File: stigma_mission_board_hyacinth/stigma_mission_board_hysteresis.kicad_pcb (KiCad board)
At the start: 4 copper layers, 50 x 150 mm, 205 parts, among them J1 DF40C-70DS-0.4V(51), J2 DF40HB(2.5)-10DS-0.4V(51), J7 SMA, J8 SMA, J9 JST-GH 4Pin, Q1 DMN2056U, Q2 DMN2056U, Q3 AOSP21321, Q4 DMN2056U, Q5 AOSP21321, Q6 DMN2056U, Q7 AOSP21321, Q8 DMN2056U, Q9 AOSP21321, U1 LAN8742A, U10 MCP2562-E-SN, U11 MCP2562-E-SN, U12 SN74HCS594, U13 INA181, U14 INA181, U15 INA181, U16 INA181, U2 INA181, U3 TPD4E1U06, U4 L7805, U5 L7805, U6 AZ1117H-ADJ, U7 AZ1117H-ADJ, U8 Ai-Thinker-Ra-01, U9 Ai-Thinker-Ra-01, Y1 25MHz

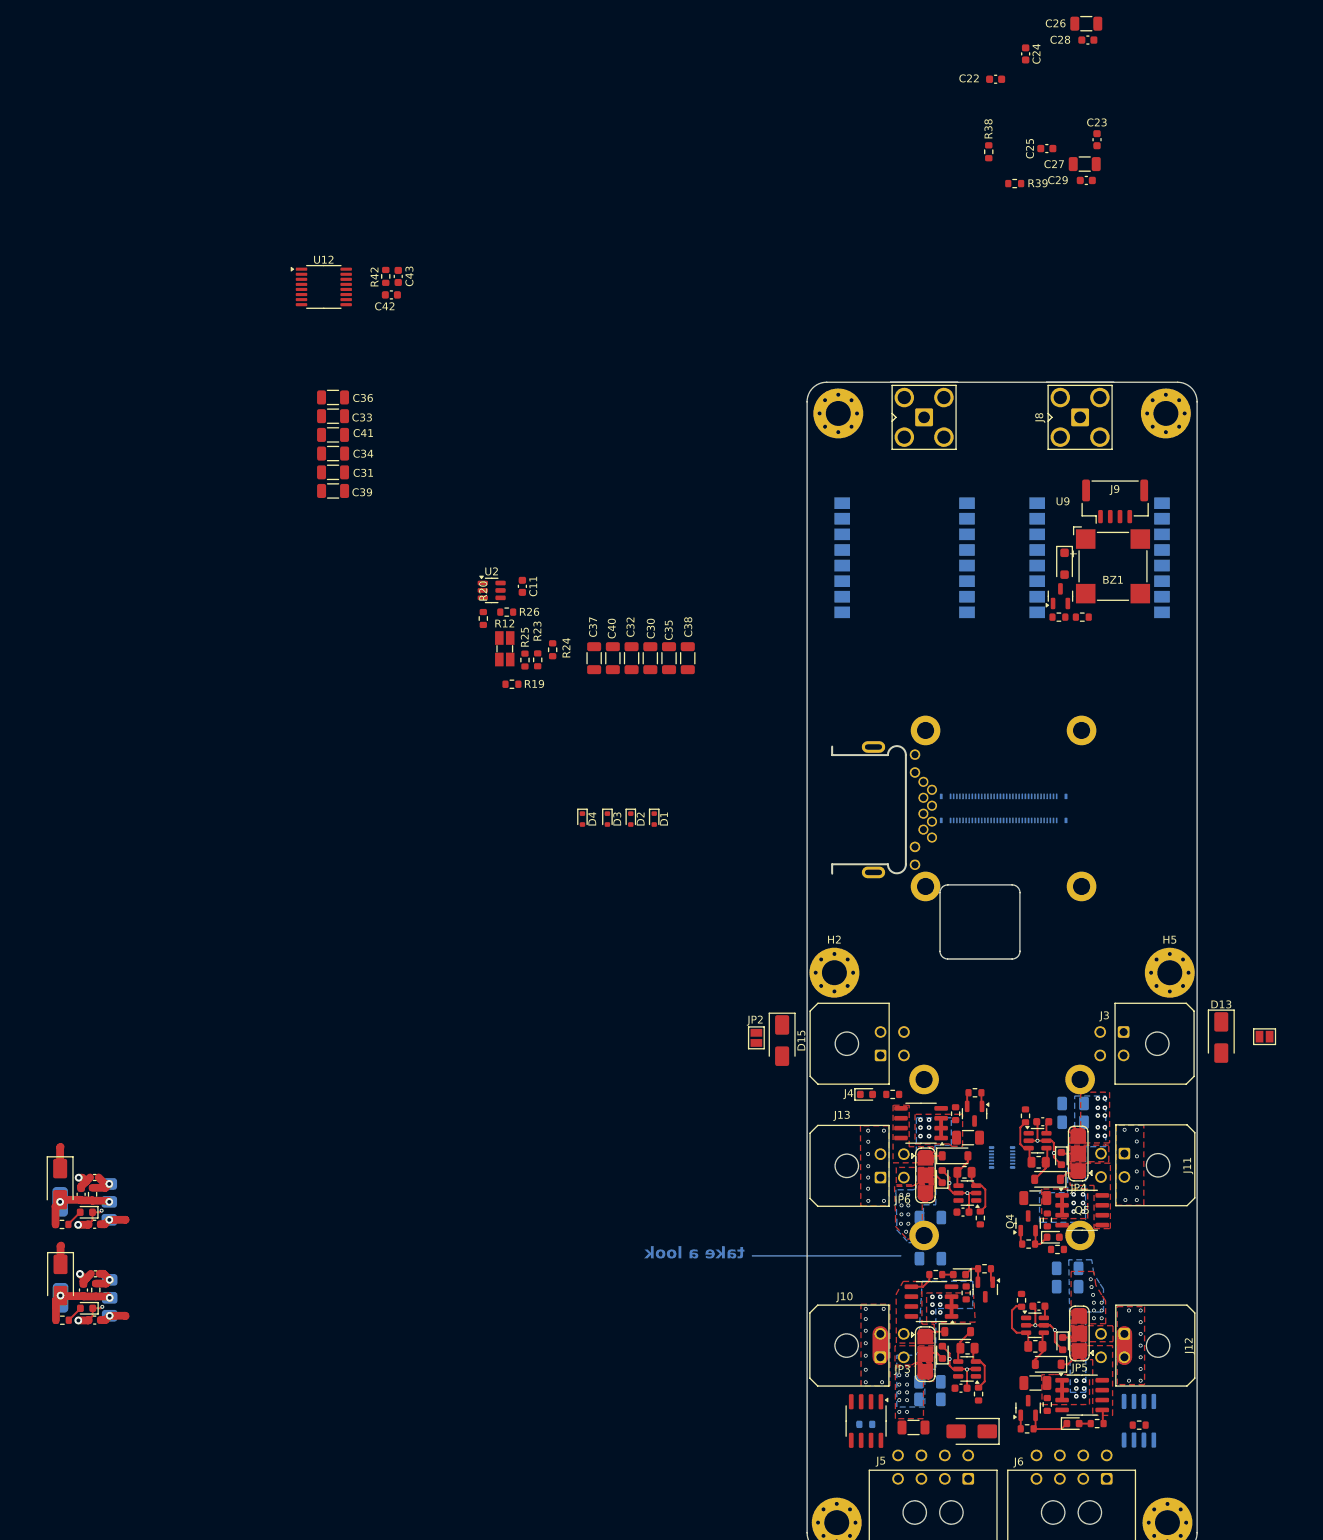
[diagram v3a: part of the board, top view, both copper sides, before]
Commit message: Layed out 3.3v regulators, buzzer, shift register and current + voltage sensing on the mission board pcb
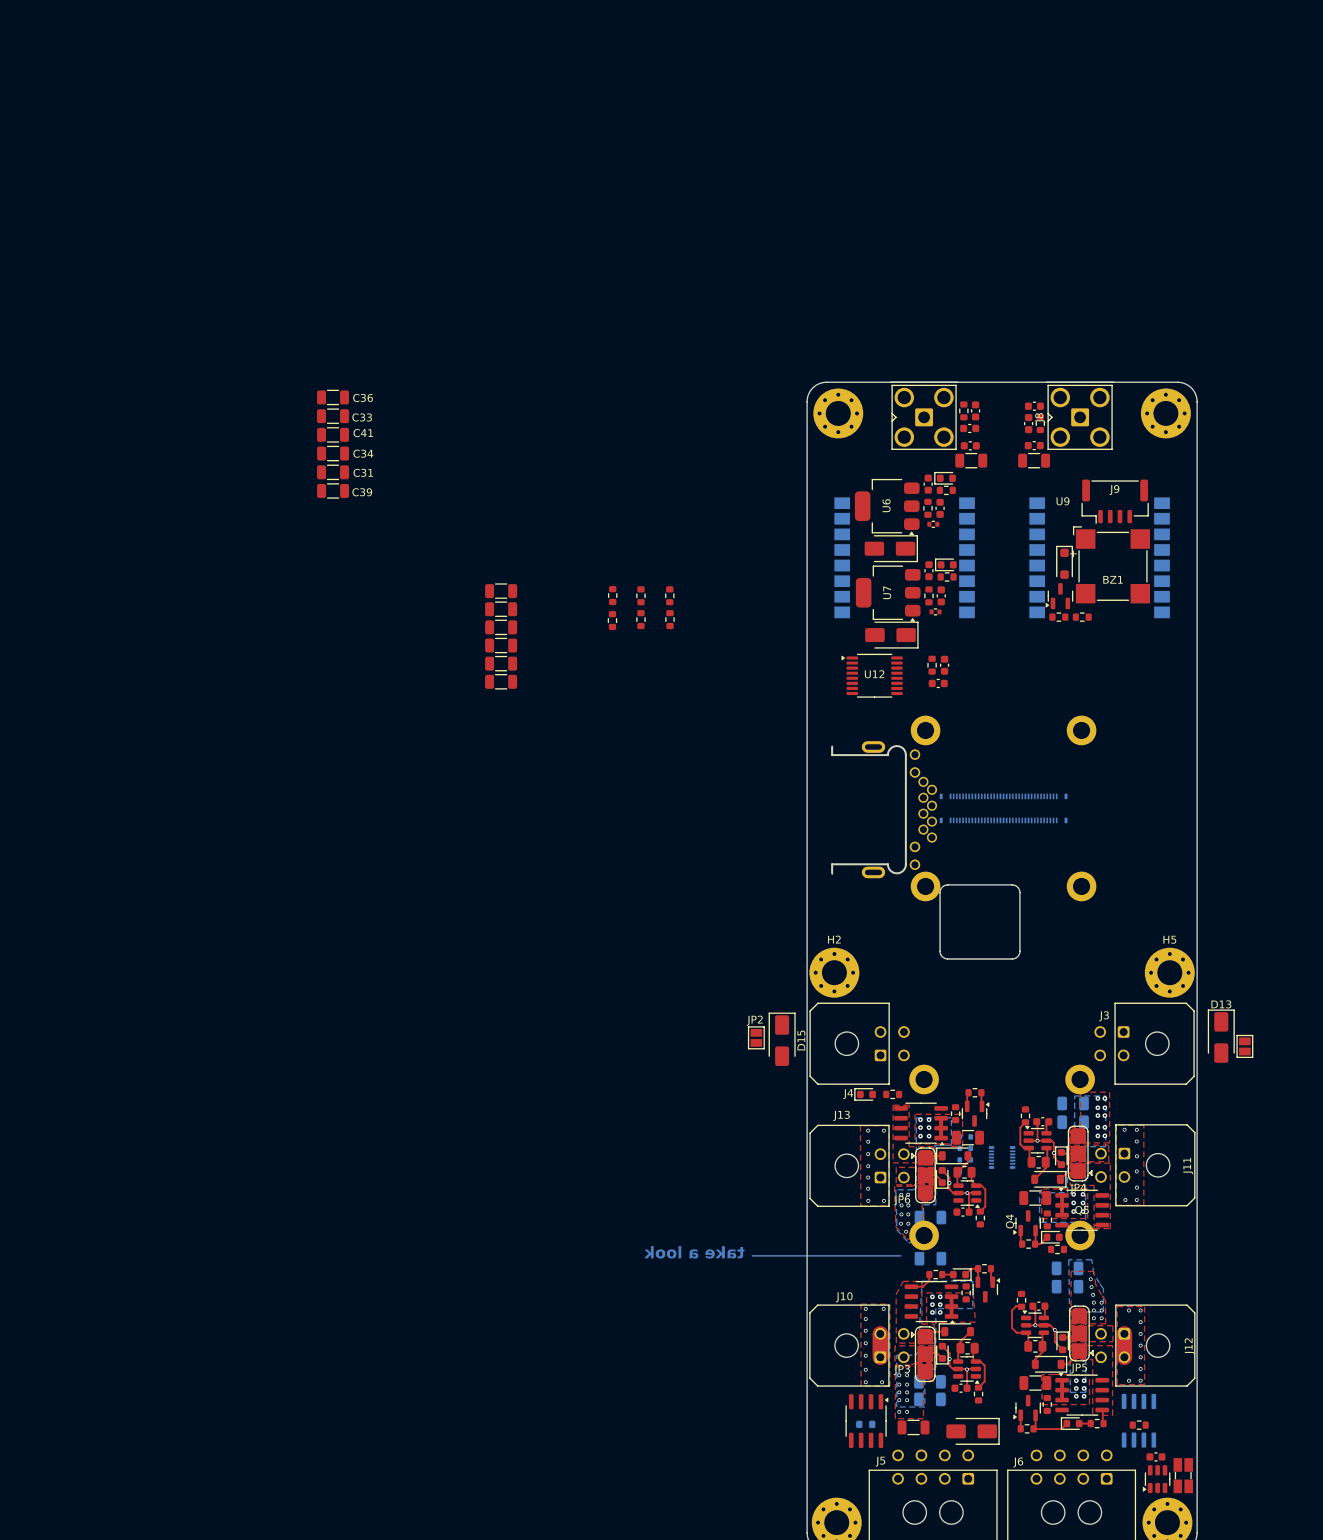
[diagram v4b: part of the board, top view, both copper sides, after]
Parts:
- D1, D2, D3, D4: moved to B.Cu
- J1: footprint Stigma:core-board -> Stigma:core-board-inner-mounting-holes
- J2: footprint Stigma:gps-board-outer-mounting-holes -> Stigma:gps-board-only-inner-mounting-holes
- U6, U7: moved to F.Cu
- moved R37 148.1 mm to (217.9, 125.0)
- moved R36 147.3 mm to (217.8, 113.9)
- moved D12 145.8 mm to (218.0, 123.4), turned to 0 degrees
- moved D11 145.0 mm to (217.9, 112.3), turned to 0 degrees
- moved C15 143.8 mm to (215.6, 124.2), turned to -90 degrees
- moved C14 142.9 mm to (215.5, 113.1), turned to -90 degrees
- moved U2 142.4 mm to (244.9, 240.6), turned to 90 degrees
- moved C21 141.5 mm to (217.2, 127.4), turned to 90 degrees
- moved C20 140.9 mm to (217.1, 116.2), turned to 90 degrees
- moved R32 139.0 mm to (215.6, 127.4), turned to -90 degrees
- moved R30 138.6 mm to (215.5, 116.2), turned to -90 degrees
- moved C11 138.0 mm to (244.7, 237.8), turned to 0 degrees
- moved R12 137.1 mm to (248.2, 240.2), turned to 180 degrees
- moved R33 137.1 mm to (216.5, 129.4), turned to 0 degrees
- moved U7 137.0 mm to (210.4, 127.0)
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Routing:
- net GND: track 88.9 -> 74.4 mm, vias 73 -> 67
- net Net-(D10-A): track 9.82 -> 0.00 mm, vias 2 -> 0
- net Net-(D9-A): track 9.81 -> 0.00 mm, vias 2 -> 0
- net +5V: track 11.8 -> 4.92 mm, vias 2 -> 0
- net +3.3V: track 8.41 -> 3.16 mm
- net Net-(U6-GND): track 4.05 -> 0.00 mm, vias 1 -> 0
- net Net-(U7-GND): track 3.61 -> 0.00 mm, vias 1 -> 0
- net Net-(D11-A): track 2.19 -> 0.00 mm
- net Net-(D12-A): track 2.15 -> 0.00 mm
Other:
- board text added: "3,3V"
- board text added: "BZR"
- board text added: "LORA"
- board text added: "sensing"
- board text added: "shift"
- board text added: "todo: symmetrize"
- board text removed: "3.3V Regulator"
- board text removed: "Das hier geht doch trotzdem nicht, oder?"
- board text removed: "GPS"
- board text removed: "LoRa Module"
- board text removed: "Shift Register IO"
- board text removed: "das hier könnte/müsste wieder {dblquote}symmetrisiert{dblquote} werden"

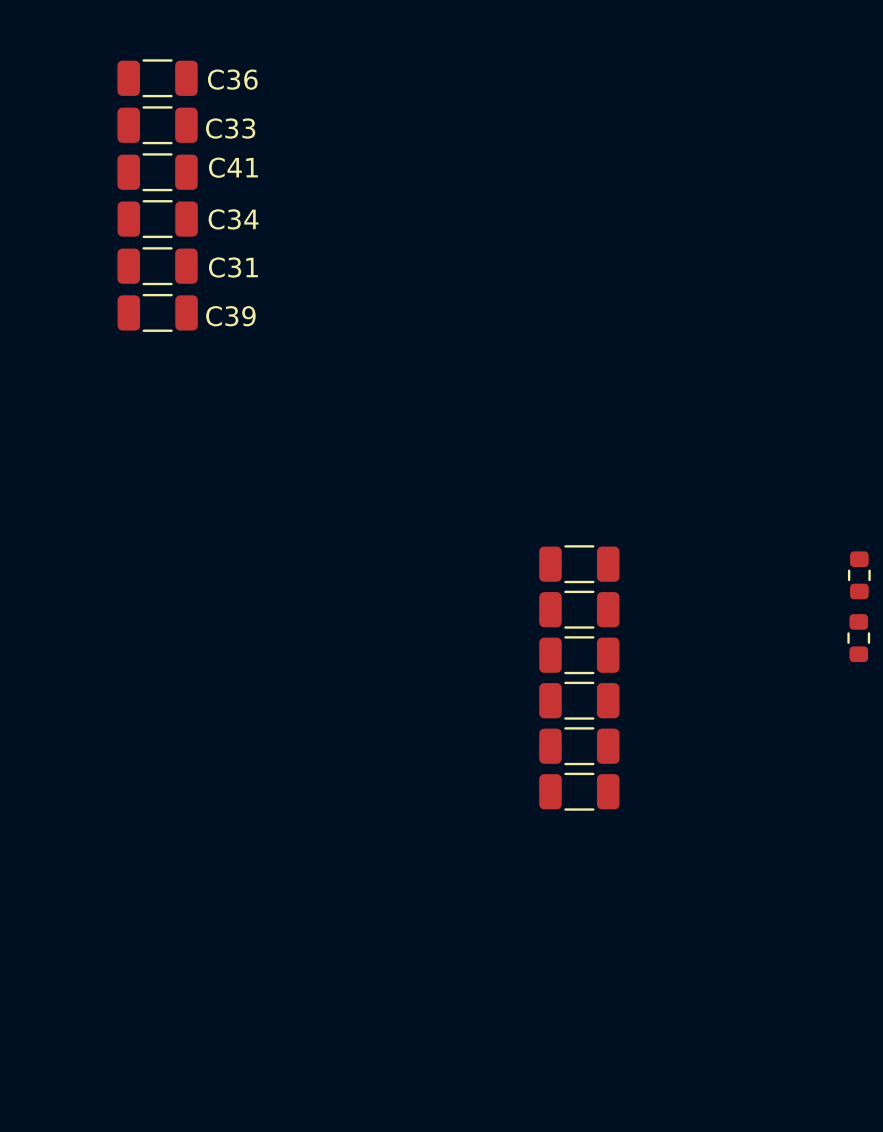
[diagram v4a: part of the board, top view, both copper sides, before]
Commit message: changed capacitors
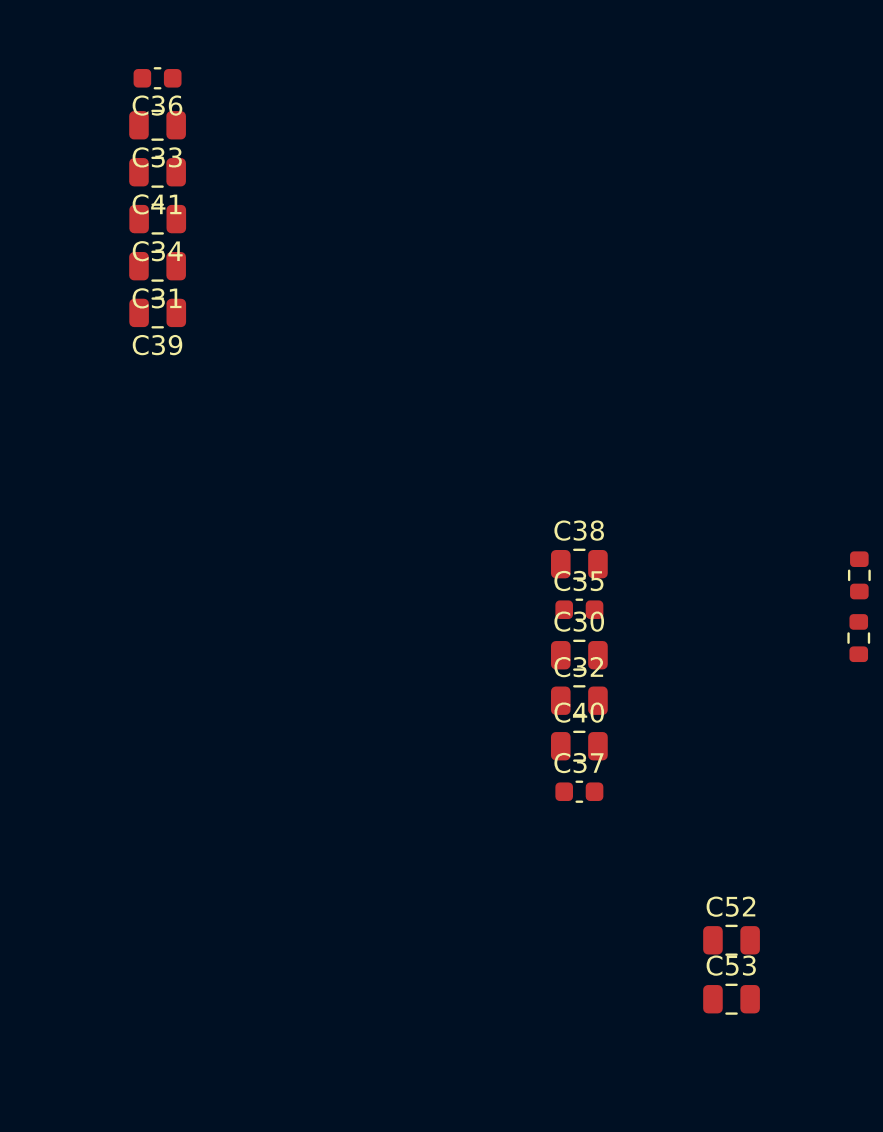
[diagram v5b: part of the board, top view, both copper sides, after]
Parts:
- added C52: 4u7, Capacitor_SMD:C_0805_2012Metric, F.Cu at (168.6, 146.0)
- added C53: 4u7, Capacitor_SMD:C_0805_2012Metric, F.Cu at (168.6, 149.0)
- C30, C32, C33, C34, C39, C40: footprint Capacitor_SMD:C_1206_3216Metric -> Capacitor_SMD:C_0805_2012Metric
- C31: value 1u -> 22u; footprint Capacitor_SMD:C_1206_3216Metric -> Capacitor_SMD:C_0805_2012Metric
- C35: footprint Capacitor_SMD:C_1206_3216Metric -> Capacitor_SMD:C_0603_1608Metric
- C36, C37: value 22u -> 1u; footprint Capacitor_SMD:C_1206_3216Metric -> Capacitor_SMD:C_0603_1608Metric
- C38: value 22u -> 10u; footprint Capacitor_SMD:C_1206_3216Metric -> Capacitor_SMD:C_0805_2012Metric
- C41: value 4u7 -> 22u; footprint Capacitor_SMD:C_1206_3216Metric -> Capacitor_SMD:C_0805_2012Metric
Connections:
- C37 pad 2: main_voltage -> high_current_2
- C38 pad 2: main_voltage -> high_current_2
- C39 pad 2: high_current -> high_current_2
- C41 pad 2: high_current -> high_current_2
